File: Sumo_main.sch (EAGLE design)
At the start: 32 parts, among them U1 ATMEGA8U2AU, U2 SN65HVD3082ED, X1 MINI-USB-SCHIELD-32005-201, X2 RS485, X4 IR Sensor 1, X5 IR Sensor 2, X6 IR Sensor 3, Y1 16MHz

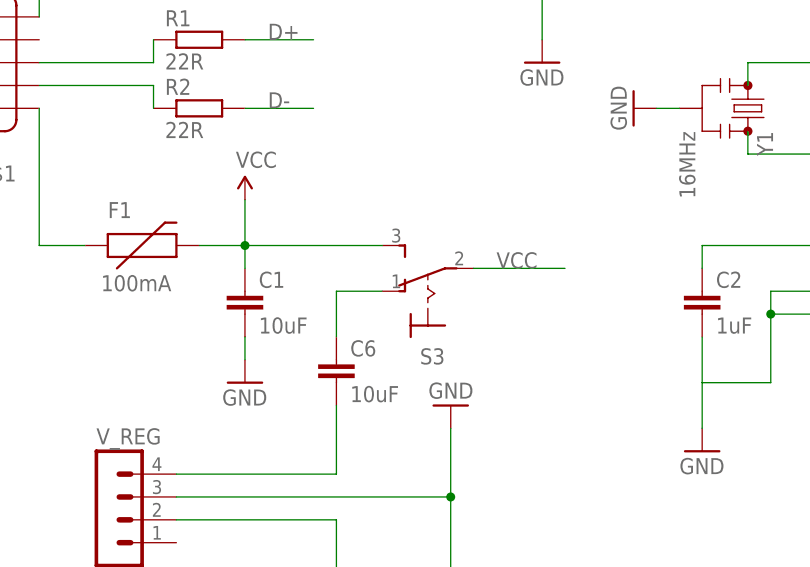
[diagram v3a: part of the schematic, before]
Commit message: Changed power switch in schematic for pin headers to connect it with wires later.
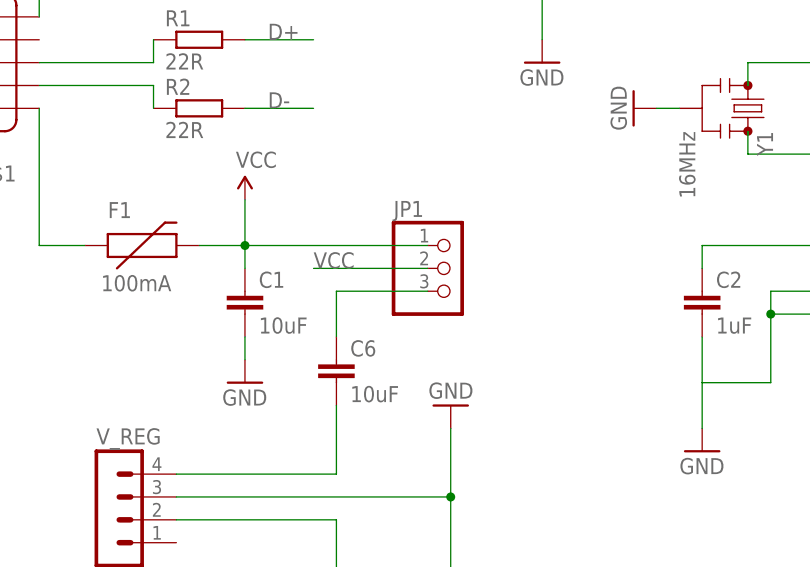
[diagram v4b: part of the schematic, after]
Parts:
- removed S3: (no value), switch:M9040P
- added JP1: (no value), pinhead:PINHD-1X3
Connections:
- net N$14: now also JP1.3; no longer S3.O
- net VCC: now also JP1.1, JP1.2; no longer S3.P, S3.S
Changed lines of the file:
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@@
 <part name="J1" library="SparkFun-Connectors" deviceset="M02" device="2.54MM_SCREWTERM"/>
 <part name="GND10" library="SparkFun-Aesthetics" deviceset="GND" device=""/>
-<part name="S3" library="switch" deviceset="M9040P" device=""/>
 <part name="C6" library="SparkFun-Capacitors" deviceset="CAP" device="0603-CAP" value="10uF"/>
 <part name="START_MODULE" library="con-lstb" deviceset="MA04-1" device=""/>
@@
 <part name="U2" library="SN65HVD3082ED" deviceset="SN65HVD3082ED" device=""/>
 <part name="GND12" library="SparkFun-Aesthetics" deviceset="GND" device=""/>
+<part name="JP1" library="pinhead" deviceset="PINHD-1X3" device=""/>
 </parts>
 <sheets>
@@
 <instance part="J1" gate="G$1" x="0" y="-10.16" rot="MR90"/>
 <instance part="GND10" gate="1" x="12.7" y="20.32" rot="R180"/>
-<instance part="S3" gate="1" x="10.16" y="33.02" rot="R90"/>
 <instance part="C6" gate="G$1" x="0" y="22.86"/>
 <instance part="START_MODULE" gate="1" x="144.78" y="50.8" rot="MR0"/>
@@
 <instance part="U2" gate="A" x="-25.4" y="104.14"/>
 <instance part="GND12" gate="1" x="-48.26" y="86.36"/>
+<instance part="JP1" gate="A" x="12.7" y="35.56"/>
 </instances>
 <busses>
@@
 <wire x1="-10.16" y1="35.56" x2="-10.16" y2="38.1" width="0.1524" layer="91"/>
 <junction x="-10.16" y="38.1"/>
-<pinref part="S3" gate="1" pin="S"/>
-<wire x1="-10.16" y1="38.1" x2="5.08" y2="38.1" width="0.1524" layer="91"/>
+<wire x1="-10.16" y1="38.1" x2="10.16" y2="38.1" width="0.1524" layer="91"/>
+<pinref part="JP1" gate="A" pin="1"/>
 </segment>
 <segment>
@@
 </segment>
 <segment>
-<pinref part="S3" gate="1" pin="P"/>
-<wire x1="15.24" y1="35.56" x2="25.4" y2="35.56" width="0.1524" layer="91"/>
-<label x="17.78" y="35.56" size="1.778" layer="95"/>
-</segment>
-<segment>
 <pinref part="START_MODULE" gate="1" pin="1"/>
 <wire x1="137.16" y1="45.72" x2="121.92" y2="45.72" width="0.1524" layer="91"/>
 <label x="124.46" y="45.72" size="1.778" layer="95"/>
+</segment>
+<segment>
+<pinref part="JP1" gate="A" pin="2"/>
+<wire x1="10.16" y1="35.56" x2="-2.54" y2="35.56" width="0.1524" layer="91"/>
+<label x="-2.54" y="35.56" size="1.778" layer="95"/>
 </segment>
 </net>
@@
 <net name="N$14" class="0">
 <segment>
-<pinref part="S3" gate="1" pin="O"/>
-<wire x1="0" y1="33.02" x2="5.08" y2="33.02" width="0.1524" layer="91"/>
 <pinref part="C6" gate="G$1" pin="1"/>
 <wire x1="0" y1="27.94" x2="0" y2="33.02" width="0.1524" layer="91"/>
-</segment>
-</net>
+<pinref part="JP1" gate="A" pin="3"/>
+<wire x1="10.16" y1="33.02" x2="0" y2="33.02" width="0.1524" layer="91"/>
+</segment>
+</net>

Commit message: Bug fixes.
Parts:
- removed C6: 10uF, SparkFun-Capacitors:CAP0603-CAP
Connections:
- removed net N$12: R8.1, X2-3.S
- removed net N$21: C6.2, V_REG.4
- new net N$16: R8.1, U2.B, X2-3.S
- net D-: now also U1.D-
- net N$11: now also U2.A
- net N$14: now also V_REG.4; no longer C6.1
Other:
- moved on the sheet: S1, S2

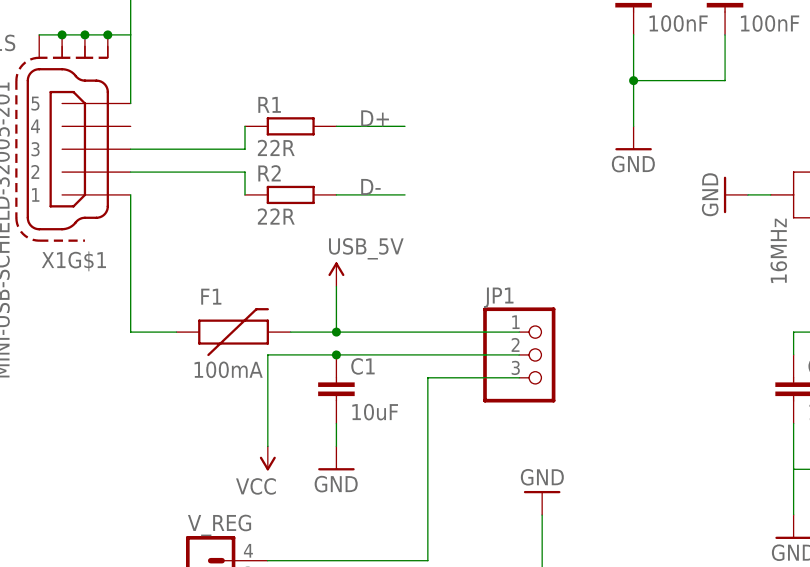
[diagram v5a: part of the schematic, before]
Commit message: Signal bug fixes.
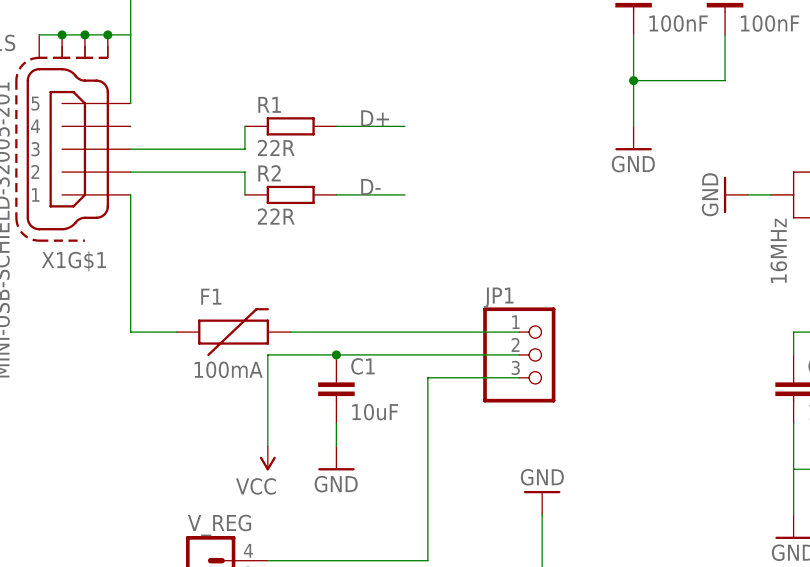
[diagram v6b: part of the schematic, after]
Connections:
- new net N$12: F1.2, JP1.1
- net VCC: no longer F1.2, JP1.1
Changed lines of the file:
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@@
 <part name="C3" library="SparkFun-Capacitors" deviceset="CAP" device="0603-CAP" value="100nF"/>
 <part name="C4" library="SparkFun-Capacitors" deviceset="CAP" device="0603-CAP" value="100nF"/>
-<part name="SUPPLY1" library="SparkFun-Aesthetics" deviceset="VCC" device="" value="USB_5V"/>
 <part name="GND1" library="SparkFun-Aesthetics" deviceset="GND" device=""/>
 <part name="GND2" library="SparkFun-Aesthetics" deviceset="GND" device=""/>
@@
 <instance part="C3" gate="G$1" x="22.86" y="73.66"/>
 <instance part="C4" gate="G$1" x="33.02" y="73.66"/>
-<instance part="SUPPLY1" gate="G$1" x="-10.16" y="43.18"/>
 <instance part="GND1" gate="1" x="-10.16" y="22.86"/>
 <instance part="GND2" gate="1" x="40.64" y="15.24"/>
@@
 <net name="VCC" class="0">
 <segment>
-<pinref part="F1" gate="G$1" pin="2"/>
-<pinref part="SUPPLY1" gate="G$1" pin="VCC"/>
-<wire x1="-15.24" y1="38.1" x2="-10.16" y2="38.1" width="0.1524" layer="91"/>
-<wire x1="-10.16" y1="38.1" x2="-10.16" y2="43.18" width="0.1524" layer="91"/>
-<junction x="-10.16" y="38.1"/>
-<wire x1="-10.16" y1="38.1" x2="10.16" y2="38.1" width="0.1524" layer="91"/>
-<pinref part="JP1" gate="A" pin="1"/>
-</segment>
-<segment>
 <pinref part="U1" gate="G$1" pin="UVCC"/>
 <wire x1="53.34" y1="71.12" x2="45.72" y2="71.12" width="0.1524" layer="91"/>
@@
 </segment>
 </net>
+<net name="N$12" class="0">
+<segment>
+<pinref part="F1" gate="G$1" pin="2"/>
+<wire x1="-15.24" y1="38.1" x2="10.16" y2="38.1" width="0.1524" layer="91"/>
+<pinref part="JP1" gate="A" pin="1"/>
+</segment>
+</net>

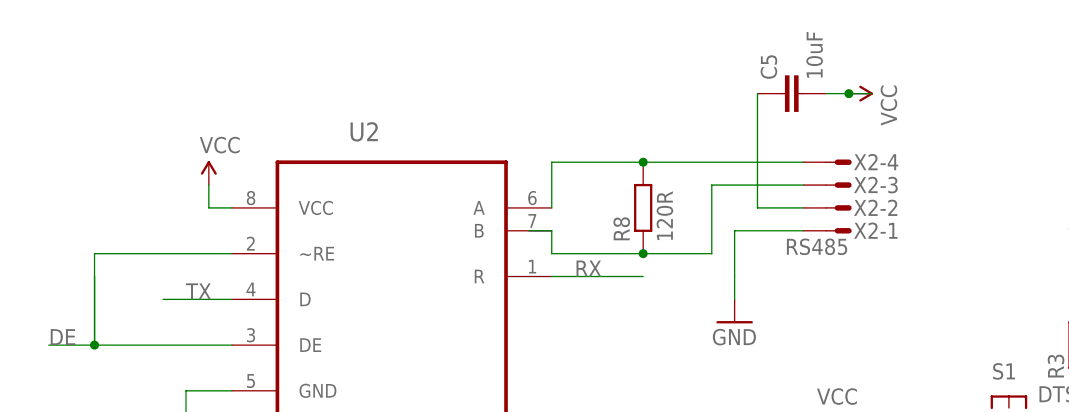
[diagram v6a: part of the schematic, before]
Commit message: Added capacitor to RS-485 chip's VCC and connected RS-485 micromatch VCC capacitor to ground.
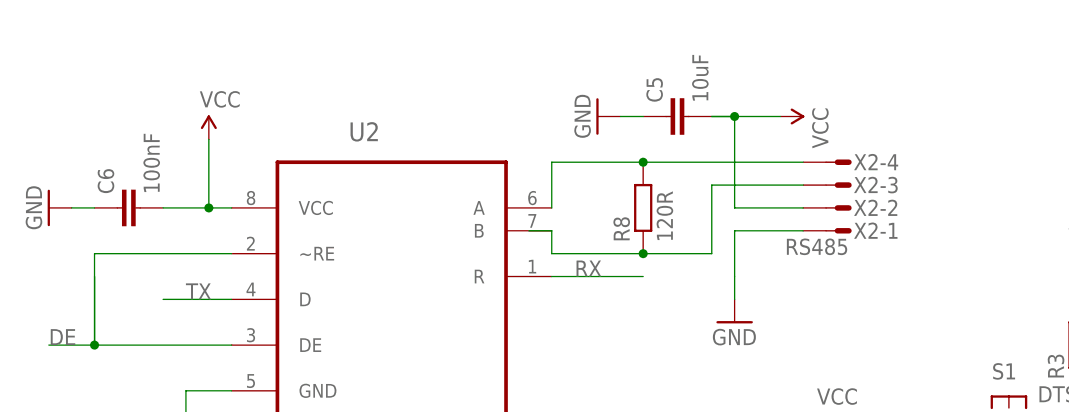
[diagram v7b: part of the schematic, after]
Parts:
- added C6: 100nF, SparkFun-Capacitors:CAP0603-CAP
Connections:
- removed net N$15: C5.1, X2-2.S
- net GND: now also C5.1, C6.1
- net VCC: now also C6.2, X2-2.S
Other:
- moved on the sheet: C5
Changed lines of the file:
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@@
 <part name="JP1" library="pinhead" deviceset="PINHD-1X3" device=""/>
 <part name="SUPPLY7" library="SparkFun-Aesthetics" deviceset="VCC" device=""/>
+<part name="GND13" library="SparkFun-Aesthetics" deviceset="GND" device=""/>
+<part name="GND14" library="SparkFun-Aesthetics" deviceset="GND" device=""/>
+<part name="C6" library="SparkFun-Capacitors" deviceset="CAP" device="0603-CAP" value="100nF"/>
 </parts>
 <sheets>
@@
 <instance part="X6" gate="-4" x="129.54" y="106.68" rot="R180"/>
 <instance part="GND9" gate="1" x="12.7" y="99.06"/>
-<instance part="SUPPLY5" gate="G$1" x="-45.72" y="114.3"/>
+<instance part="SUPPLY5" gate="G$1" x="-45.72" y="119.38"/>
 <instance part="R8" gate="G$1" x="2.54" y="111.76" rot="R90"/>
 <instance part="X2" gate="-1" x="25.4" y="109.22" rot="R180"/>
@@
 <instance part="X2" gate="-3" x="25.4" y="114.3" rot="R180"/>
 <instance part="X2" gate="-4" x="25.4" y="116.84" rot="R180"/>
-<instance part="C5" gate="G$1" x="20.32" y="124.46" rot="R90"/>
-<instance part="SUPPLY6" gate="G$1" x="25.4" y="124.46" rot="R270"/>
+<instance part="C5" gate="G$1" x="7.62" y="121.92" rot="R90"/>
+<instance part="SUPPLY6" gate="G$1" x="17.78" y="121.92" rot="R270"/>
 <instance part="J1" gate="G$1" x="0" y="-10.16" rot="MR90"/>
 <instance part="GND10" gate="1" x="12.7" y="20.32" rot="R180"/>
@@
 <instance part="JP1" gate="A" x="12.7" y="35.56"/>
 <instance part="SUPPLY7" gate="G$1" x="-17.78" y="25.4" rot="R180"/>
+<instance part="GND13" gate="1" x="-2.54" y="121.92" rot="R270"/>
+<instance part="GND14" gate="1" x="-63.5" y="111.76" rot="R270"/>
+<instance part="C6" gate="G$1" x="-53.34" y="111.76" rot="R90"/>
 </instances>
 <busses>
@@
 </segment>
 <segment>
-<wire x1="-45.72" y1="111.76" x2="-45.72" y2="114.3" width="0.1524" layer="91"/>
-<pinref part="SUPPLY5" gate="G$1" pin="VCC"/>
-<pinref part="U2" gate="A" pin="VCC"/>
-<wire x1="-45.72" y1="111.76" x2="-43.18" y2="111.76" width="0.1524" layer="91"/>
-</segment>
-<segment>
-<pinref part="C5" gate="G$1" pin="2"/>
-<wire x1="22.86" y1="124.46" x2="25.4" y2="124.46" width="0.1524" layer="91"/>
-<pinref part="SUPPLY6" gate="G$1" pin="VCC"/>
-<wire x1="25.4" y1="124.46" x2="27.94" y2="124.46" width="0.1524" layer="91"/>
-<junction x="25.4" y="124.46"/>
-</segment>
-<segment>
 <pinref part="START_MODULE" gate="1" pin="1"/>
 <wire x1="137.16" y1="45.72" x2="121.92" y2="45.72" width="0.1524" layer="91"/>
@@
 <junction x="-10.16" y="35.56"/>
 <pinref part="SUPPLY7" gate="G$1" pin="VCC"/>
+</segment>
+<segment>
+<pinref part="C6" gate="G$1" pin="2"/>
+<pinref part="SUPPLY5" gate="G$1" pin="VCC"/>
+<wire x1="-50.8" y1="111.76" x2="-45.72" y2="111.76" width="0.1524" layer="91"/>
+<wire x1="-45.72" y1="111.76" x2="-45.72" y2="119.38" width="0.1524" layer="91"/>
+<pinref part="U2" gate="A" pin="VCC"/>
+<wire x1="-45.72" y1="111.76" x2="-43.18" y2="111.76" width="0.1524" layer="91"/>
+<junction x="-45.72" y="111.76"/>
+</segment>
+<segment>
+<pinref part="X2" gate="-2" pin="S"/>
+<wire x1="20.32" y1="111.76" x2="12.7" y2="111.76" width="0.1524" layer="91"/>
+<wire x1="12.7" y1="111.76" x2="12.7" y2="121.92" width="0.1524" layer="91"/>
+<pinref part="C5" gate="G$1" pin="2"/>
+<wire x1="12.7" y1="121.92" x2="10.16" y2="121.92" width="0.1524" layer="91"/>
+<pinref part="SUPPLY6" gate="G$1" pin="VCC"/>
+<wire x1="10.16" y1="121.92" x2="12.7" y2="121.92" width="0.1524" layer="91"/>
+<junction x="12.7" y="121.92"/>
+<wire x1="12.7" y1="121.92" x2="17.78" y2="121.92" width="0.1524" layer="91"/>
 </segment>
 </net>
@@
 <wire x1="-10.16" y1="25.4" x2="-10.16" y2="27.94" width="0.1524" layer="91"/>
 </segment>
+<segment>
+<pinref part="GND14" gate="1" pin="GND"/>
+<pinref part="C6" gate="G$1" pin="1"/>
+<wire x1="-60.96" y1="111.76" x2="-58.42" y2="111.76" width="0.1524" layer="91"/>
+</segment>
+<segment>
+<pinref part="GND13" gate="1" pin="GND"/>
+<pinref part="C5" gate="G$1" pin="1"/>
+<wire x1="0" y1="121.92" x2="2.54" y2="121.92" width="0.1524" layer="91"/>
+</segment>
 </net>
 <net name="N$5" class="0">
@@
 </segment>
 </net>
-<net name="N$15" class="0">
-<segment>
-<pinref part="X2" gate="-2" pin="S"/>
-<wire x1="20.32" y1="111.76" x2="15.24" y2="111.76" width="0.1524" layer="91"/>
-<wire x1="15.24" y1="111.76" x2="15.24" y2="124.46" width="0.1524" layer="91"/>
-<pinref part="C5" gate="G$1" pin="1"/>
-</segment>
-</net>
